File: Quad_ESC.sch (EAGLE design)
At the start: 23 parts, among them U1 SN74CBTLV3257PWR, Y1 ECS-80-S-4X

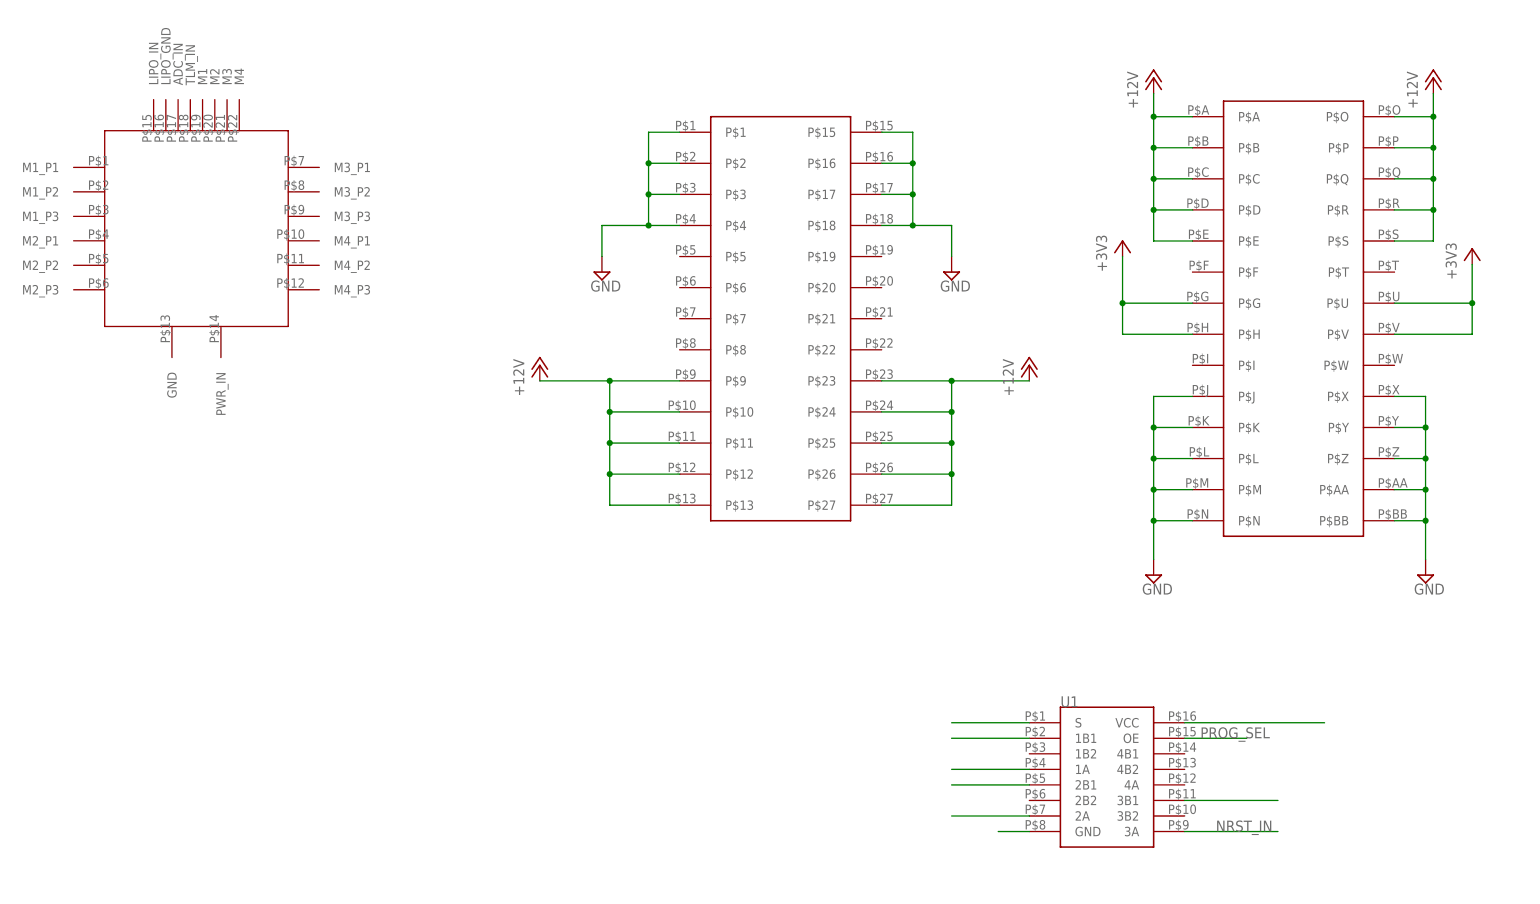
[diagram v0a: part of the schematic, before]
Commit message: Lib Changes/Schem Update
Added Cutouts/changed dimensions of ESC footprint in library; added board parts to library; tweaked schematic; created board file.
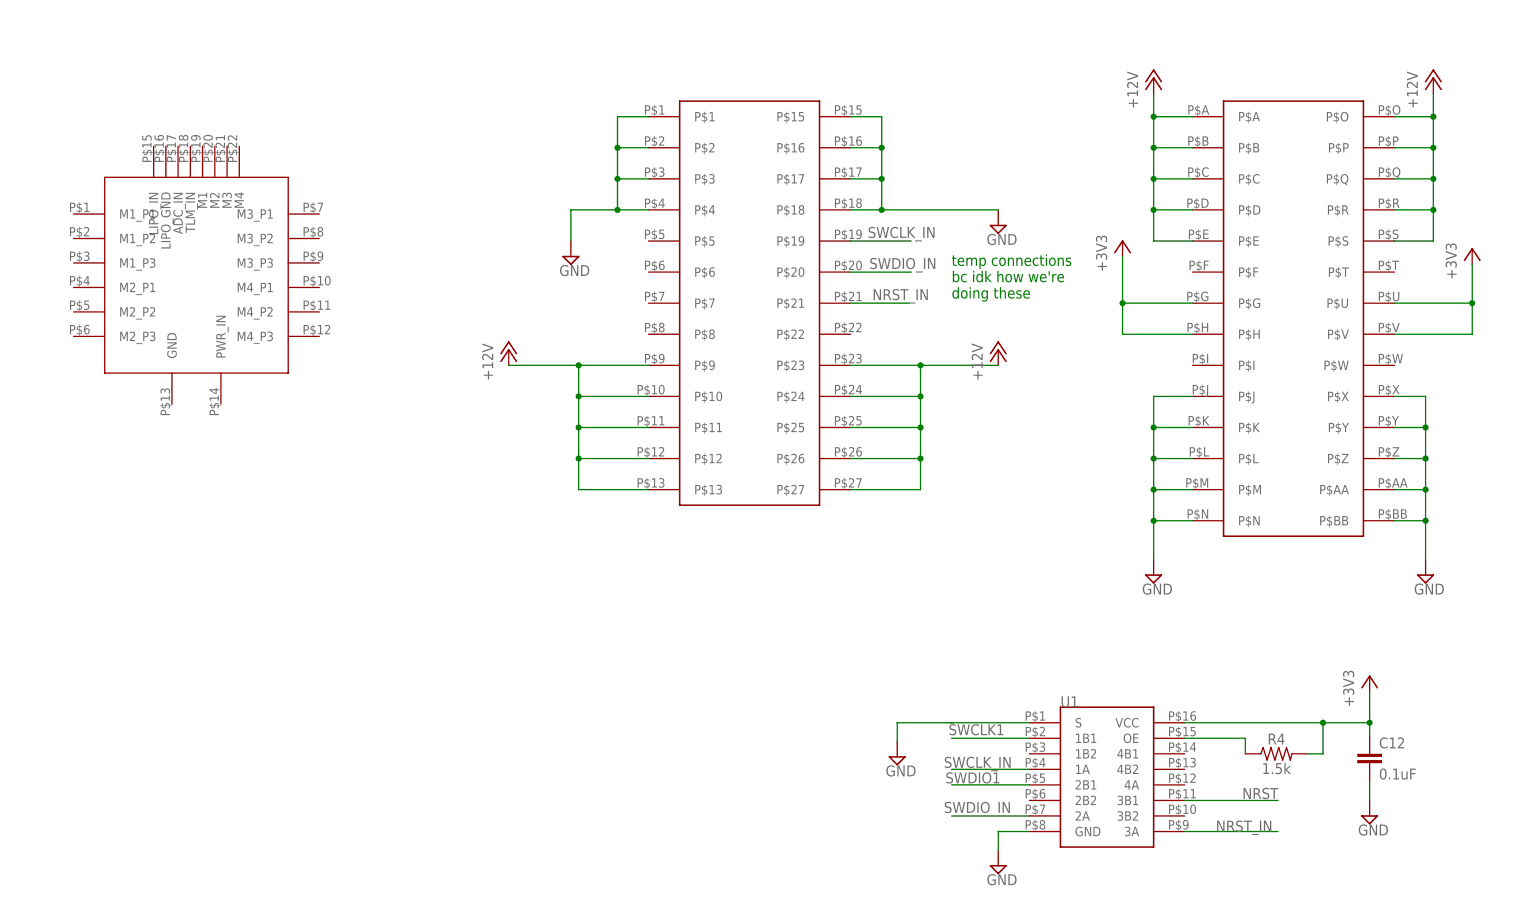
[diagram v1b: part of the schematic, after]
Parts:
- added C12: 0.1uF, SparkFun-Capacitors:0.1UF-0603-25V-(+80/-20%)
- added R4: 1.5k, SparkFun-Resistors:1.5KOHM-0603-1/10W-1%
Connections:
- removed net +3V1: U1.VCC
- removed net GND1: U1.GND, U1.S
- removed net PROG_SEL: U1.OE
- new net N$3: R4.1, U1.OE
- net +3V3: now also C12.1, R4.2, U1.VCC
- net GND: now also C12.2, U1.GND, U1.S
- net NRST_IN: now also U$2G$1.P$21
- net SWCLK_IN: now also U$2G$1.P$19
- net SWDIO_IN: now also U$2G$1.P$20
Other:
- note added: "temp connections bc idk how we're doing these"

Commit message: Lib Update (again)
ok definitely did not push the wrong version of the library file last time haha
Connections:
- net NRST_IN: no longer U$2G$1.P$21
- net SWCLK_IN: no longer U$2G$1.P$19
- net SWDIO_IN: no longer U$2G$1.P$20
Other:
- note removed: "temp connections bc idk how we're doing these"
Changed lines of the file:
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@@
 <text x="354.33" y="76.2" size="1.778" layer="91">CAN TRANSCEIVER</text>
 <text x="474.98" y="78.74" size="1.778" layer="91">OSCILLATOR</text>
-<text x="179.07" y="129.032" size="1.778" layer="91">temp connections
-bc idk how we're
-doing these</text>
 </plain>
 <instances>
@@
 <attribute name="VALUE" x="114.935" y="132.715" size="1.778" layer="96"/>
 </instance>
-<instance part="SUPPLY4" gate="GND" x="186.69" y="140.97" smashed="yes">
-<attribute name="VALUE" x="184.785" y="137.795" size="1.778" layer="96"/>
-</instance>
+<instance part="SUPPLY4" gate="GND" x="186.69" y="140.97" smashed="yes"/>
 <instance part="U$1" gate="G$1" x="40.64" y="116.84" smashed="yes"/>
 </instances>
@@
 <label x="177.8" y="52.324" size="1.778" layer="95"/>
 </segment>
-<segment>
-<pinref part="U$2" gate="G$1" pin="P$19"/>
-<wire x1="162.56" y1="138.43" x2="172.466" y2="138.43" width="0.1524" layer="91"/>
-<label x="165.354" y="138.938" size="1.778" layer="95"/>
-</segment>
 </net>
 <net name="SWDIO_IN" class="0">
@@
 <label x="177.8" y="44.958" size="1.778" layer="95"/>
 </segment>
-<segment>
-<pinref part="U$2" gate="G$1" pin="P$20"/>
-<wire x1="162.56" y1="133.35" x2="172.466" y2="133.35" width="0.1524" layer="91"/>
-<label x="165.608" y="133.858" size="1.778" layer="95"/>
-</segment>
 </net>
 <net name="NRST_IN" class="0">
@@
 <wire x1="217.17" y1="41.91" x2="232.41" y2="41.91" width="0.1524" layer="91"/>
 <label x="222.25" y="41.91" size="1.778" layer="95"/>
-</segment>
-<segment>
-<pinref part="U$2" gate="G$1" pin="P$21"/>
-<wire x1="162.56" y1="128.27" x2="172.212" y2="128.27" width="0.1524" layer="91"/>
-<label x="166.116" y="128.778" size="1.778" layer="95"/>
 </segment>
 </net>
@@
 </drawing>
 <compatibility>
-<note version="6.3" minversion="6.2.2" severity="warning">
-Since Version 6.2.2 text objects can contain more than one line,
-which will not be processed correctly with this version.
-</note>
 <note version="8.2" severity="warning">
 Since Version 8.2, EAGLE supports online libraries. The ids

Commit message: Lib Update/Sch Update
Migrated 3 pin connectors from X-11 AFRO lib; fixed BLHeli symbol so labels no longer overlap; fixed connections and placement on schematic.
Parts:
- added SV2: (no value), con-lsta:FE05-1
- added U$5, U$6, U$7: 3PINCONNECTOR, BLHeli_32 45A:3PINCONNECTOR
- added U$9: BL_HELI45A, BLHeli_32 45A:BL_HELI45A
- U$1: value BL_HELI45A -> 3PINCONNECTOR; device BLHeli_32 45A:BL_HELI45A -> BLHeli_32 45A:3PINCONNECTOR
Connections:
- new net ESC1_B: U$1.A, U$9.M1_P1
- new net ESC1_R: U$1.C, U$9.M1_P3
- new net ESC1_Y: U$1.B, U$9.M1_P2
- new net ESC2_B: U$5.A, U$9.M2_P1
- new net ESC2_R: U$5.C, U$9.M2_P3
- new net ESC2_Y: U$5.B, U$9.M2_P2
- new net ESC3_B: U$6.A, U$9.M3_P1
- new net ESC3_R: U$6.C, U$9.M3_P3
- new net ESC3_Y: U$6.B, U$9.M3_P2
- new net ESC4_B: U$7.A, U$9.M4_P1
- new net ESC4_R: U$7.C, U$9.M4_P3
- new net ESC4_Y: U$7.B, U$9.M4_P2
- new net N$31: U$9.ADC
- new net N$32: U$9.TLM/RX2
- new net TIM3_CH1: U$4.PA6, U$9.MTR_1
- new net TIM3_CH2: U$4.PA7, U$9.MTR_2
- new net TIM3_CH3: U$4.PB0, U$9.MTR_3
- new net TIM3_CH4: U$4.PB1, U$9.MTR_4
- net +12V: now also U$9.+12V
- net +3V3: now also SV2.5
- net GND: now also SV2.3, U$9.GND, U$9.LIPO_GND, U$9.LIPO_IN
- net NRST_IN: now also SV2.1
- net SWCLK_IN: now also SV2.4
- net SWDIO_IN: now also SV2.2
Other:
- moved on the sheet: C10, C12, R4, U$8, U1

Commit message: Board Update
Added minor pin connections
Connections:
- removed net N$3: R4.1, U1.OE
- new net PROG_SEL: R4.1, U$2G$1.P$5, U1.OE
- net CAN_H: now also U$2G$1.P$6
- net CAN_L: now also U$2G$1.P$7
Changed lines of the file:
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@@
 <attribute name="VALUE" x="166.37" y="120.65" size="1.778" layer="96" rot="R90"/>
 </instance>
-<instance part="SUPPLY3" gate="GND" x="99.06" y="140.97" smashed="yes">
-<attribute name="VALUE" x="97.155" y="137.795" size="1.778" layer="96"/>
+<instance part="SUPPLY3" gate="GND" x="88.9" y="140.97" smashed="yes">
+<attribute name="VALUE" x="86.995" y="137.795" size="1.778" layer="96"/>
 </instance>
 <instance part="SUPPLY4" gate="GND" x="168.91" y="146.05" smashed="yes"/>
@@
 <wire x1="111.76" y1="158.75" x2="106.68" y2="158.75" width="0.1524" layer="91"/>
 <junction x="106.68" y="158.75"/>
-<wire x1="106.68" y1="148.59" x2="99.06" y2="148.59" width="0.1524" layer="91"/>
+<wire x1="106.68" y1="148.59" x2="88.9" y2="148.59" width="0.1524" layer="91"/>
 <junction x="106.68" y="148.59"/>
-<wire x1="99.06" y1="148.59" x2="99.06" y2="143.51" width="0.1524" layer="91"/>
+<wire x1="88.9" y1="148.59" x2="88.9" y2="143.51" width="0.1524" layer="91"/>
 <pinref part="SUPPLY3" gate="GND" pin="GND"/>
 </segment>
@@
 </segment>
 </net>
-<net name="N$3" class="0">
+<net name="PROG_SEL" class="0">
 <segment>
 <pinref part="U1" gate="G$1" pin="OE"/>
@@
 <wire x1="217.17" y1="62.23" x2="227.076" y2="62.23" width="0.1524" layer="91"/>
 <wire x1="227.076" y1="62.23" x2="227.076" y2="59.69" width="0.1524" layer="91"/>
+<label x="220.218" y="62.484" size="1.778" layer="95"/>
+</segment>
+<segment>
+<pinref part="U$2" gate="G$1" pin="P$5"/>
+<wire x1="111.76" y1="143.51" x2="96.52" y2="143.51" width="0.1524" layer="91"/>
+<label x="96.266" y="143.51" size="1.778" layer="95"/>
 </segment>
 </net>
@@
 <label x="425.45" y="53.34" size="1.778" layer="95"/>
 </segment>
+<segment>
+<pinref part="U$2" gate="G$1" pin="P$6"/>
+<wire x1="111.76" y1="138.43" x2="96.52" y2="138.43" width="0.1524" layer="91"/>
+<label x="96.012" y="138.43" size="1.778" layer="95"/>
+</segment>
 </net>
 <net name="CAN_L" class="0">
@@
 <label x="425.45" y="48.26" size="1.778" layer="95"/>
 </segment>
-</net>
+<segment>
+<wire x1="111.76" y1="133.35" x2="96.52" y2="133.35" width="0.1524" layer="91"/>
+<pinref part="U$2" gate="G$1" pin="P$7"/>
+<label x="96.52" y="133.35" size="1.778" layer="95"/>
+</segment>
+</net>

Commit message: Lib/Schem Update
tweaked connections to STM chip; split esc device into lumenier ESC and 8 pin connector (need to figure out how to pair those still :/ ); scooted around components on schematic
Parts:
- removed C12: 0.1uF, SparkFun-Capacitors:0.1UF-0603-25V-(+80/-20%)
- removed R4: 1.5k, SparkFun-Resistors:1.5KOHM-0603-1/10W-1%
- removed U1: SN74CBTLV3257PWR, SN74CBTLV3257PWR:SN74CBTLV3257PWR
- added U$10: BL_HELI45A, BLHeli_32 45A:BL_HELI45A
- U$9: value BL_HELI45A -> 8PIN_CONNECTOR; device BLHeli_32 45A:BL_HELI45A -> BLHeli_32 45A:8PIN_CONNECTOR
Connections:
- removed net N$31: U$9.ADC
- removed net N$32: U$9.TLM/RX2
- removed net NRST_IN: SV2.1, U1.3A
- removed net SWCLK1: U1.1B1
- removed net SWCLK_IN: SV2.4, U1.1A
- removed net SWDIO1: U1.2B1
- removed net SWDIO_IN: SV2.2, U1.2A
- new net N$6: U$9.TLM
- net +12V: now also U$10.+12V; no longer U$9.+12V
- net +3V3: no longer C12.1, R4.2, U1.VCC
- net ESC1_B: now also U$10.M1_P1, U$9.ADC; no longer U$9.M1_P1
- net ESC1_R: now also U$10.M1_P3; no longer U$9.M1_P3
- net ESC1_Y: now also U$10.M1_P2; no longer U$9.M1_P2
- net ESC2_B: now also U$10.M2_P1; no longer U$9.M2_P1
- net ESC2_R: now also U$10.M2_P3; no longer U$9.M2_P3
- net ESC2_Y: now also U$10.M2_P2; no longer U$9.M2_P2
- net ESC3_B: now also U$10.M3_P1; no longer U$9.M3_P1
- net ESC3_R: now also U$10.M3_P3; no longer U$9.M3_P3
- net ESC3_Y: now also U$10.M3_P2; no longer U$9.M3_P2
- net ESC4_B: now also U$10.M4_P1; no longer U$9.M4_P1
- net ESC4_R: now also U$10.M4_P3; no longer U$9.M4_P3
- net ESC4_Y: now also U$10.M4_P2; no longer U$9.M4_P2
- net GND: now also U$10.GND; no longer C12.2, U$9.GND, U1.GND, U1.S
- net NRST: now also SV2.1; no longer U1.3B1
- net PROG_SEL: no longer R4.1, U1.OE
- net SWCLK: now also SV2.4
- net SWDIO: now also SV2.2
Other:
- note added: "BACKPLANE CONNECTIONS"
- note added: "LUMENIER ESC & 8 PIN CONNECTOR"
- note added: "M1 3 Pin"
- note added: "M2 3 Pin"
- note added: "M3 3 Pin"
- note added: "M4 3 Pin"
- note added: "MOTOR 3PIN CONNECTORS"
- note added: "PROGRAMMING HEADERS"
- moved on the sheet: C1, C10, C2, C3, C4, C5, C6, C7, C8, C9, D1, R1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

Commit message: Schem/Lib Update
added new footprint to schematic and library, added ID resistor to chip, standardized symbols across schematic
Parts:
- added R4: 10k, SparkFun-Resistors:10KOHM-0603-1/10W-1%
- R7: value 470 -> (none)
- U$10: value BL_HELI45A -> LUMENIER_QUAD; device BLHeli_32 45A:BL_HELI45A -> BLHeli_32 45A:LUMENIER_QUAD
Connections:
- removed net OSC_IN1: U$4.PF0-OSC_IN
- removed net OSC_OUT1: U$4.PF1-OSC_OUT
- new net 3.3V: R4.1
- net +12V: now also U$10.VIN; no longer U$10.+12V
- net ESC1_B: now also U$10.M1P1; no longer U$10.M1_P1
- net ESC1_R: now also U$10.M1P3; no longer U$10.M1_P3
- net ESC1_Y: now also U$10.M1P2; no longer U$10.M1_P2
- net ESC2_B: now also U$10.M2P1; no longer U$10.M2_P1
- net ESC2_R: now also U$10.M2P3; no longer U$10.M2_P3
- net ESC2_Y: now also U$10.M2P2; no longer U$10.M2_P2
- net ESC3_B: now also U$10.M3P1; no longer U$10.M3_P1
- net ESC3_R: now also U$10.M3P3; no longer U$10.M3_P3
- net ESC3_Y: now also U$10.M3P2; no longer U$10.M3_P2
- net ESC4_B: now also U$10.M4P1; no longer U$10.M4_P1
- net ESC4_R: now also U$10.M4P3; no longer U$10.M4_P3
- net ESC4_Y: now also U$10.M4P2; no longer U$10.M4_P2
- net GND: now also R4.2, U$4.PA3
- net OSC_IN: now also U$4.PF0-OSC_IN
- net OSC_OUT: now also U$4.PF1-OSC_OUT
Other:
- note added: "ID resistor to backplane"
- moved on the sheet: C1

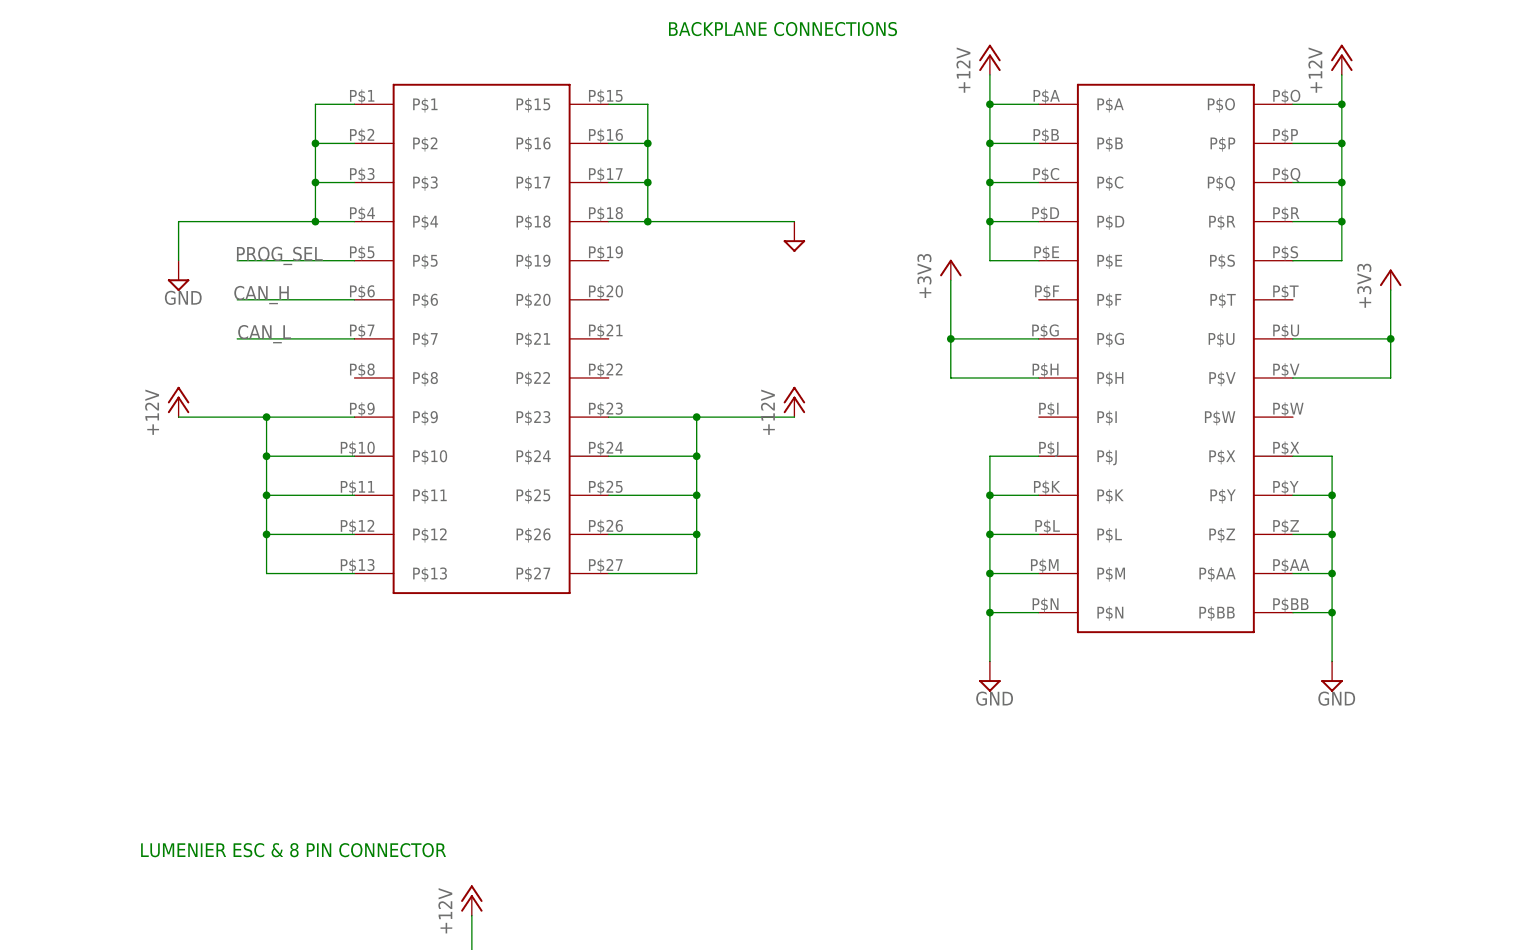
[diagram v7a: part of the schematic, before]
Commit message: Minor Sch Fixes/Board Placement
Fixed issues with schematic and doubling of backplane connectors, precursory board placements and connections
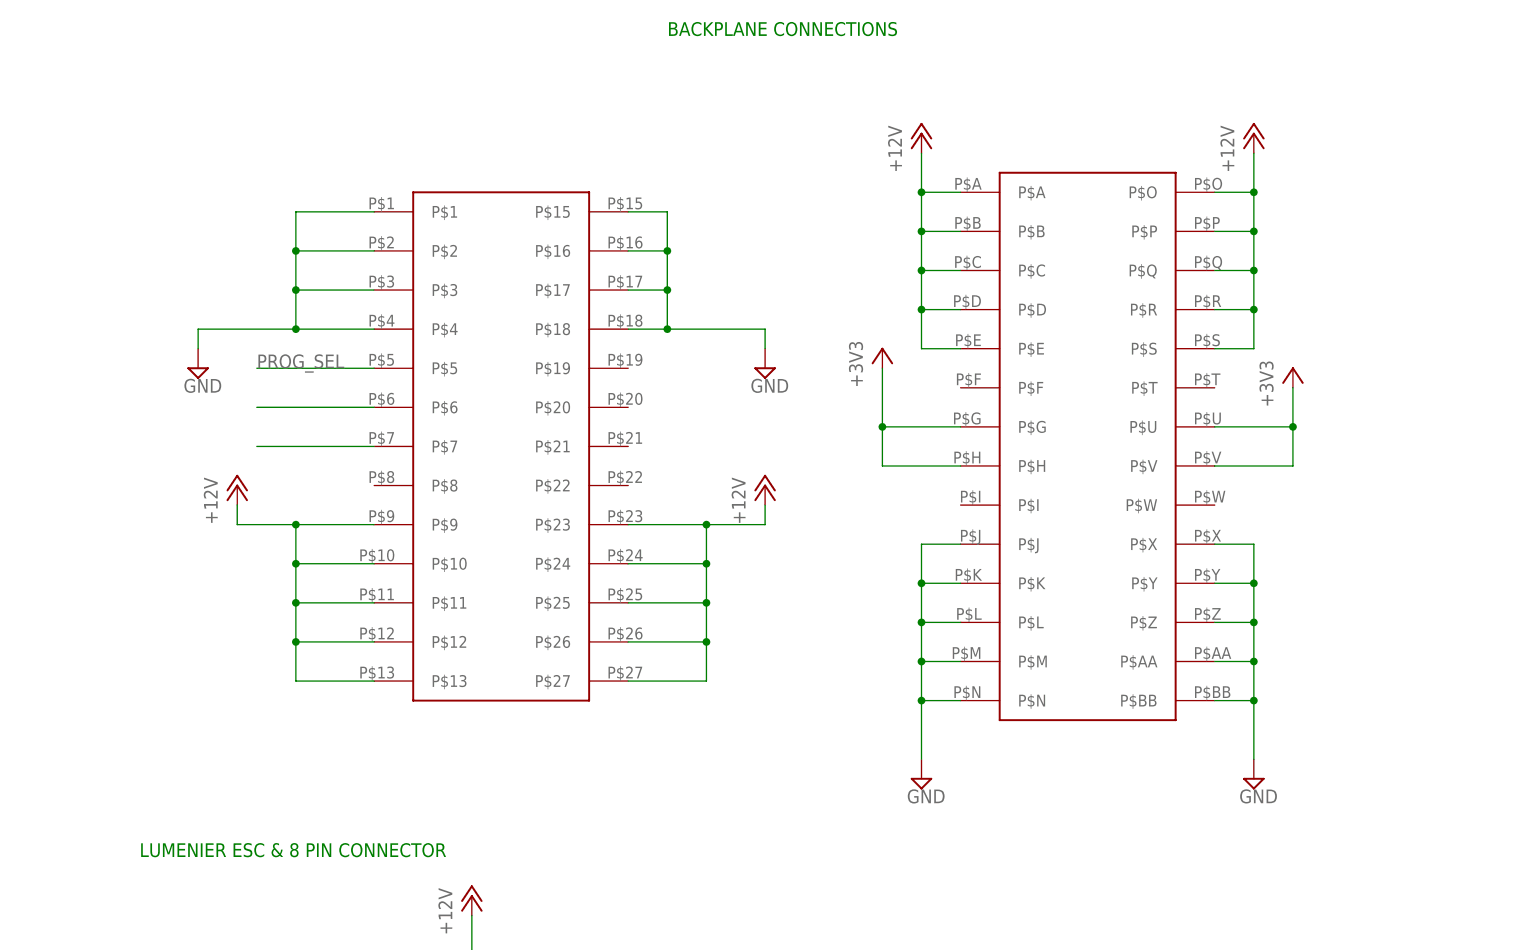
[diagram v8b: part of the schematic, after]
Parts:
- removed U$3: ESC2BACKPLANE, ESC_to_Backplane_Connectors:ESC2BACKPLANE
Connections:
- new net N$10: U$2G$1.P$7
- new net N$9: U$2G$1.P$6
- net +12V: now also U$2G$2.P$A, U$2G$2.P$B, U$2G$2.P$C, U$2G$2.P$D, U$2G$2.P$E, U$2G$2.P$O, U$2G$2.P$P, U$2G$2.P$Q, U$2G$2.P$R, U$2G$2.P$S; no longer U$3G$2.P$A, U$3G$2.P$B, U$3G$2.P$C, U$3G$2.P$D, U$3G$2.P$E, U$3G$2.P$O, U$3G$2.P$P, U$3G$2.P$Q, U$3G$2.P$R, U$3G$2.P$S
- net +3V3: now also U$2G$2.P$G, U$2G$2.P$H, U$2G$2.P$U, U$2G$2.P$V; no longer U$3G$2.P$G, U$3G$2.P$H, U$3G$2.P$U, U$3G$2.P$V
- net CAN_H: no longer U$2G$1.P$6
- net CAN_L: no longer U$2G$1.P$7
- net GND: now also U$2G$2.P$AA, U$2G$2.P$BB, U$2G$2.P$J, U$2G$2.P$K, U$2G$2.P$L, U$2G$2.P$M, U$2G$2.P$N, U$2G$2.P$X, U$2G$2.P$Y, U$2G$2.P$Z; no longer U$3G$2.P$AA, U$3G$2.P$BB, U$3G$2.P$J, U$3G$2.P$K, U$3G$2.P$L, U$3G$2.P$M, U$3G$2.P$N, U$3G$2.P$X, U$3G$2.P$Y, U$3G$2.P$Z
